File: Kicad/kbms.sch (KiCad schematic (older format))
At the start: 24 parts, among them J1001 2x3 Header, J1002 1x3 UART Debug Header, J1003 Double-mini-DIN-6, J1004 AVR-ISP-6, SW1001 SW_Push_DPDT_ON_MO, U1001 MCP23017_SP, U1002 ATmega328P-PU

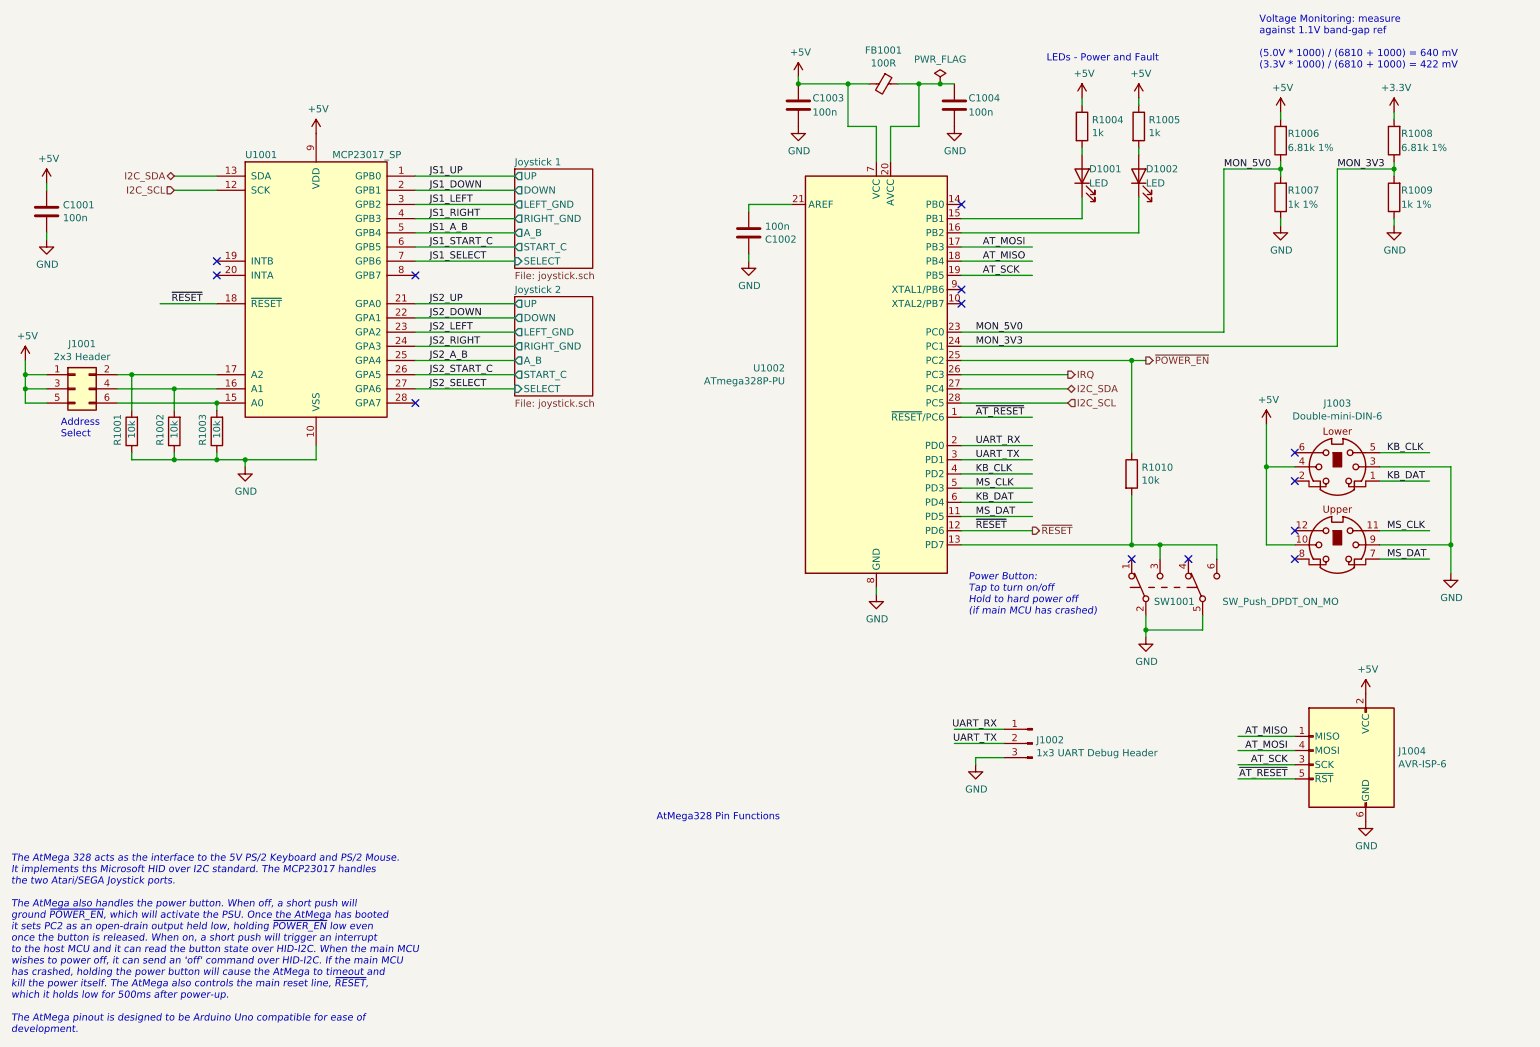
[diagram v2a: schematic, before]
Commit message: Moved Joystick controller onto its own sheet.
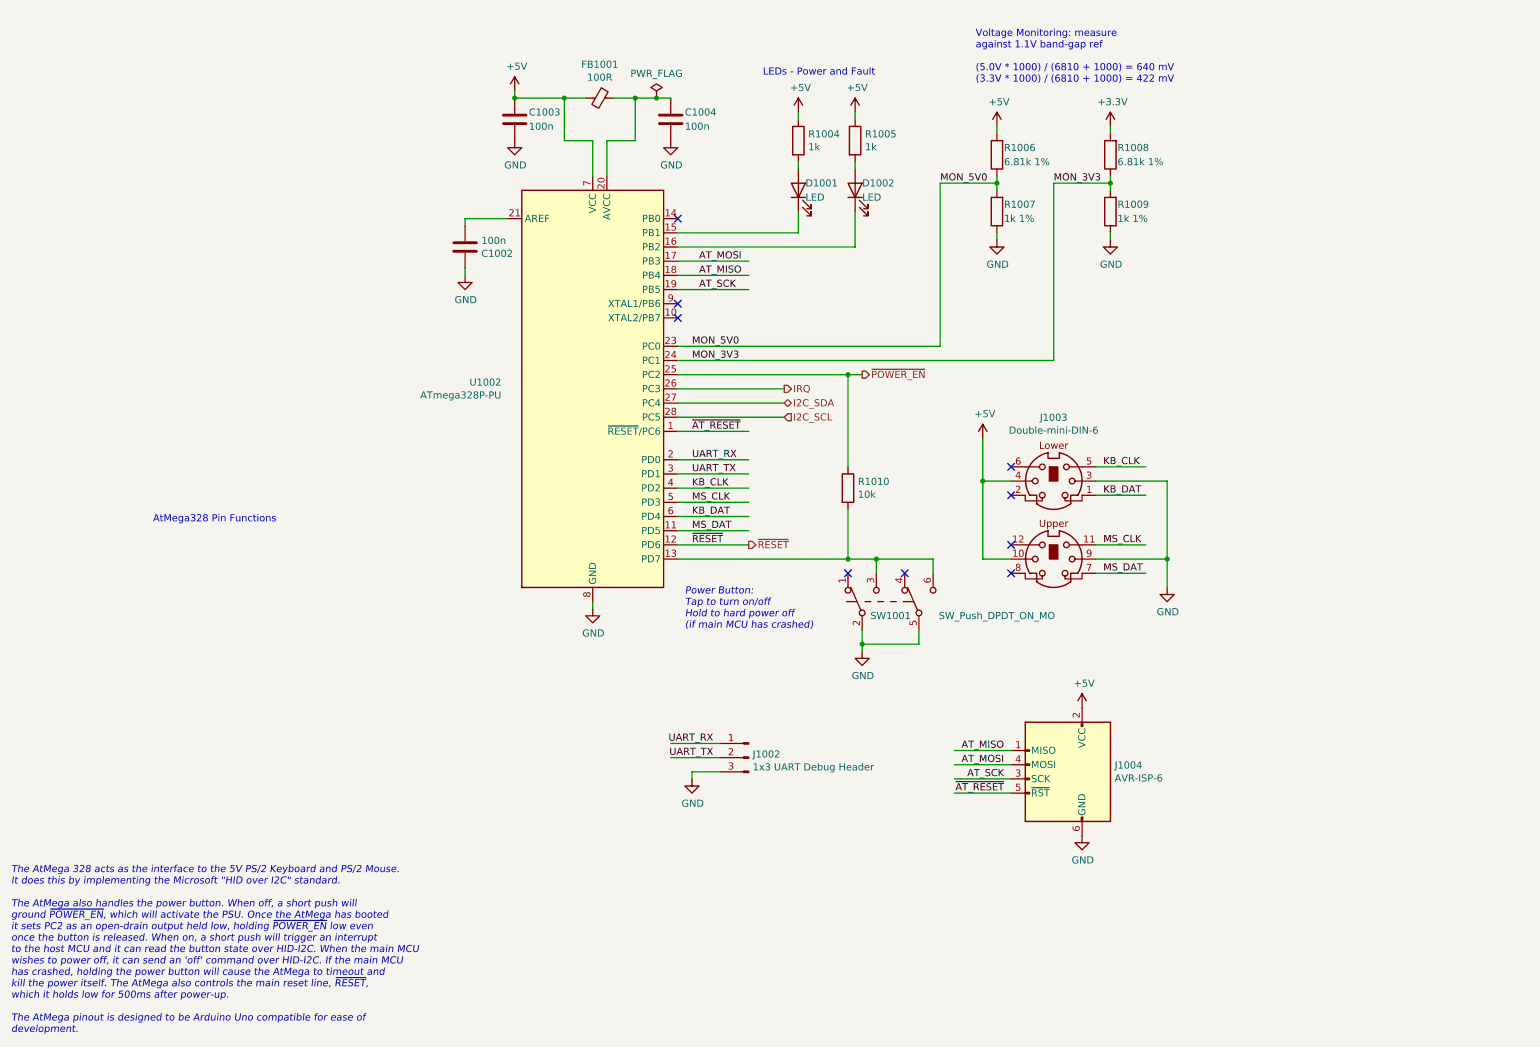
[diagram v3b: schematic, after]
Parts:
- removed C1001: 100n, Capacitor_THT:C_Disc_D3.0mm_W2.0mm_P2.50mm, symbol Device:C
- removed J1001: 2x3 Header, Connector_PinHeader_2.54mm:PinHeader_2x03_P2.54mm_Vertical, symbol Connector_Generic:Conn_02x03_Odd_Even
- removed R1001, R1002, R1003: 10k, Resistor_THT:R_Axial_DIN0207_L6.3mm_D2.5mm_P10.16mm_Horizontal, symbol Device:R
- removed U1001: MCP23017_SP, Package_DIP:DIP-28_W7.62mm, symbol Interface_Expansion:MCP23017_SP
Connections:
- net labels removed: JS1_A_B, JS1_DOWN, JS1_LEFT, JS1_RIGHT, JS1_SELECT, JS1_START_C, JS1_UP, JS2_A_B, JS2_DOWN, JS2_LEFT, JS2_RIGHT, JS2_SELECT, JS2_START_C, JS2_UP
- wire segments 127 -> 85
- no-connect marks 13 -> 9
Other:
- note added: "The AtMega 328 acts as the interface to the 5V PS/2 Keyboard and PS/2 Mouse.\nIt does this by implementing the Microsoft "HID over I2C" standard.\n\nThe AtMega also handles the power button. When off, a short push will\nground ~POWER_EN~, which will activate the PSU. Once the AtMega has booted\nit sets PC2 as an open-drain output held low, holding ~POWER_EN~ low even\nonce the button is released.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"
- note removed: "Address\nSelect"
- note removed: "The AtMega 328 acts as the interface to the 5V PS/2 Keyboard and PS/2 Mouse.\nIt implements ths Microsoft HID over I2C standard. The MCP23017 handles\nthe two Atari/SEGA Joystick ports.\n\nThe AtMega also handles the power button. When off, a short push will\nground ~POWER_EN~, which will activate the PSU. Once the AtMega has booted\nit sets PC2 as an open-drain output held low, holding ~POWER_EN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"
- moved on the sheet: C1002, C1003, C1004, D1001, D1002, FB1001, J1002, J1003, J1004, R1004, R1005, R1006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
